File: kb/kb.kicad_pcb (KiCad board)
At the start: 2 copper layers, 109 parts, among them J1 Conn_01x04_MountingPin, SW1 SW_Push, SW10 SW_Push, SW11 SW_Push, SW12 SW_Push, SW13 SW_Push, SW14 SW_Push, SW15 SW_Push, SW16 SW_Push, SW17 SW_Push, SW18 SW_Push, SW19 SW_Push, SW2 SW_Push, SW20 SW_Push, SW21 SW_Push, SW22 SW_Push, SW23 SW_Push, SW24 SW_Push, SW25 SW_Push, SW26 SW_Push, SW27 SW_Push, SW28 SW_Push, SW29 SW_Push, SW3 SW_Push, SW30 SW_Push, SW31 SW_Push, SW32 SW_Push, SW33 SW_Push, SW34 SW_Push, SW35 SW_Push, SW36 SW_Push, SW37 SW_Push, SW38 SW_Push, SW39 SW_Push, SW4 SW_Push, SW40 SW_Push, SW41 SW_Push, SW42 SW_Push, SW43 SW_Push, SW44 SW_Push, SW45 SW_Push, SW46 SW_Push, SW48 SW_Push, SW5 SW_Push, SW6 SW_Push, SW7 SW_Push, SW8 SW_Push, SW9 SW_Push, U1 USBLC6-2SC6, U2 STM32G474CETx, U4 XC6206PxxxMR

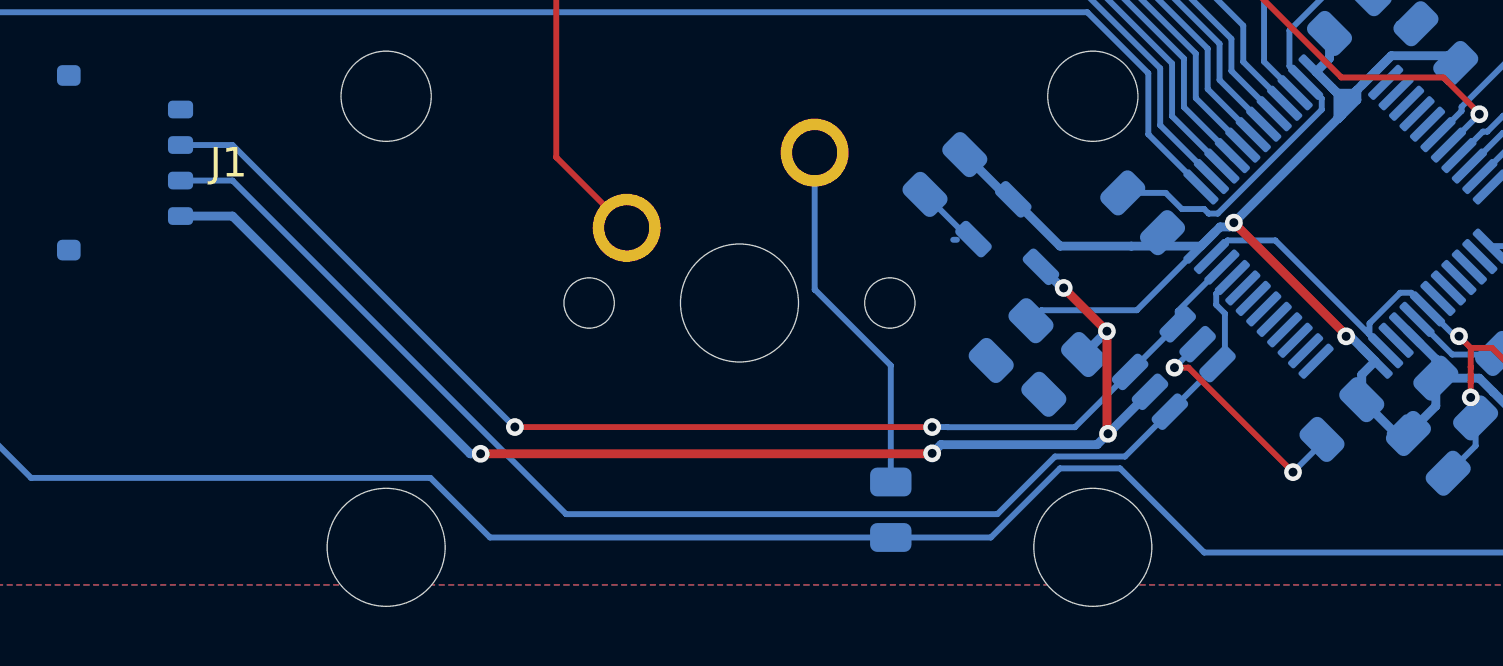
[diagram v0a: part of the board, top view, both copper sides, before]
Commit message: Removed ESD component
Due to built-in ESD functionality on daughterboard, onboard ESD protection is unnecessary
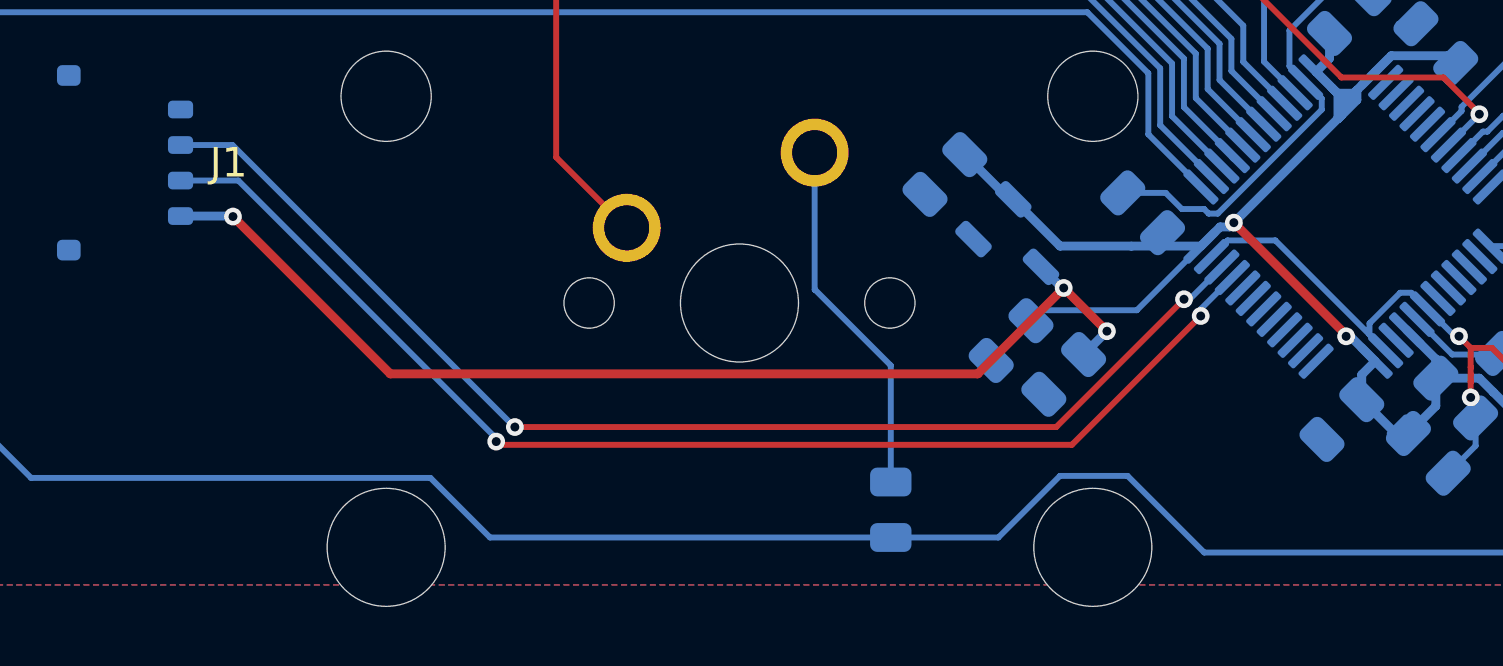
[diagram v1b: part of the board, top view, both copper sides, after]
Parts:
- removed U1: USBLC6-2SC6, Package_TO_SOT_SMD:SOT-23-6
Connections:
- C11 pad 2: (no net) -> GND
- C12 pad 2: (no net) -> GND
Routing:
- net GND: track 47.4 -> 37.1 mm, vias 5 -> 3
- net +5V: track 44.7 -> 37.5 mm, vias 5 -> 3
- net D-: track 45.2 -> 41.8 mm, vias 0 -> 2

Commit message: Added NSRT, Fixed Pins
Fixed boot pin and reset pin assignments, rerouted accordingly
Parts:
- moved C4 20.2 mm to (202.3, 102.4), turned to 180 degrees
- moved C10 18.3 mm to (195.6, 101.6), turned to 135 degrees
- moved C9 8.92 mm to (192.8, 101.6), turned to 135 degrees
- moved D42 8.87 mm to (181.0, 93.6)
- moved U4 8.85 mm to (190.1, 98.8), turned to -135 degrees
- moved J1 4.04 mm to (155.8, 93.5)
- moved C1 1.04 mm to (202.7, 98.9), turned to 45 degrees
- moved C5 1.02 mm to (187.5, 93.2), turned to -135 degrees
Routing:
- net GND: track 37.1 -> 53.2 mm
- net ROW3: track 255.9 -> 264.8 mm, vias 0 -> 2
- net +3V3: track 187.4 -> 179.5 mm, vias 4 -> 5
- net Net-(D42-A): track 12.2 -> 5.64 mm
- net D-: track 41.8 -> 36.2 mm, vias 2 -> 0
- net D+: track 41.4 -> 36.1 mm, vias 2 -> 0
- net ROW2: track 231.5 -> 235.1 mm
- net ROW0: track 280.6 -> 282.3 mm
- net Net-(U2-VREF+): track 6.61 -> 7.71 mm
- net COL0: track 219.9 -> 220.8 mm
- net +5V: track 37.5 -> 36.8 mm, vias 3 -> 0
- net ROW1: track 251.4 -> 250.8 mm

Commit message: Shrunk passive footprints
Switched footprint of passives from 0805  to 0402 and rewired accordingly
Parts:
- added C6: 100nF, Capacitor_SMD:C_0402_1005Metric, B.Cu at (198.1, 88.1)
- added SW47: RESET, Button_Switch_SMD:SW_SPST_SKQG_WithStem, B.Cu at (271.4, 33.9)
- C1, C10, C11, C12, C13, C2, C3, C4, C5, C8, C9: footprint Capacitor_SMD:C_0805_2012Metric -> Capacitor_SMD:C_0402_1005Metric
- R5: footprint Resistor_SMD:R_0805_2012Metric -> Resistor_SMD:R_0402_1005Metric
- SW48: value SW_Push -> BOOT
- moved R5 60.6 mm to (241.9, 30.5), turned to -90 degrees
- moved SW48 25.0 mm to (247.4, 34.3)
- moved C4 8.76 mm to (194.3, 98.8), turned to 0 degrees
- moved C1 4.11 mm to (199.6, 96.2), turned to -45 degrees
- moved C10 3.81 mm to (192.3, 99.7), turned to 45 degrees
- moved C9 2.74 mm to (190.1, 101.0)
- moved C3 2.69 mm to (194.7, 86.1)
- moved C12 2.18 mm to (197.6, 98.2)
- moved C13 2.17 mm to (196.3, 98.9), turned to -45 degrees
- moved C8 1.40 mm to (198.9, 96.9)
- moved C2 1.26 mm to (193.5, 86.4), turned to 135 degrees
- moved C11 0.95 mm to (198.2, 97.5)
- moved C5 0.95 mm to (188.4, 93.1)
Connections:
- U2 pad 13: ROW3 -> ROW2
- U2 pad 31: unconnected-(U2-PA9-Pad31) -> ROW3
- U2 pad 44: ROW0 -> COL7
- U2 pad 45: ROW1 -> BOOT
- U2 pad 46: ROW2 -> ROW1
- U2 pad 7: BOOT -> RESET
- U2 pad 8: COL7 -> ROW0
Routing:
- net RESET: track 0.00 -> 133.5 mm
- net GND: track 53.2 -> 30.4 mm, vias 3 -> 1
- net +3V3: track 179.5 -> 162.6 mm, vias 5 -> 4
- net BOOT: track 131.8 -> 123.3 mm, vias 0 -> 2
- net ROW0: track 282.3 -> 274.0 mm
- net ROW3: track 264.8 -> 257.1 mm, vias 2 -> 3
- net COL7: track 67.8 -> 61.4 mm
- net ROW2: track 235.1 -> 239.4 mm, vias 0 -> 2
- net Net-(U2-VREF+): track 7.71 -> 3.53 mm
- net +5V: track 36.8 -> 34.6 mm

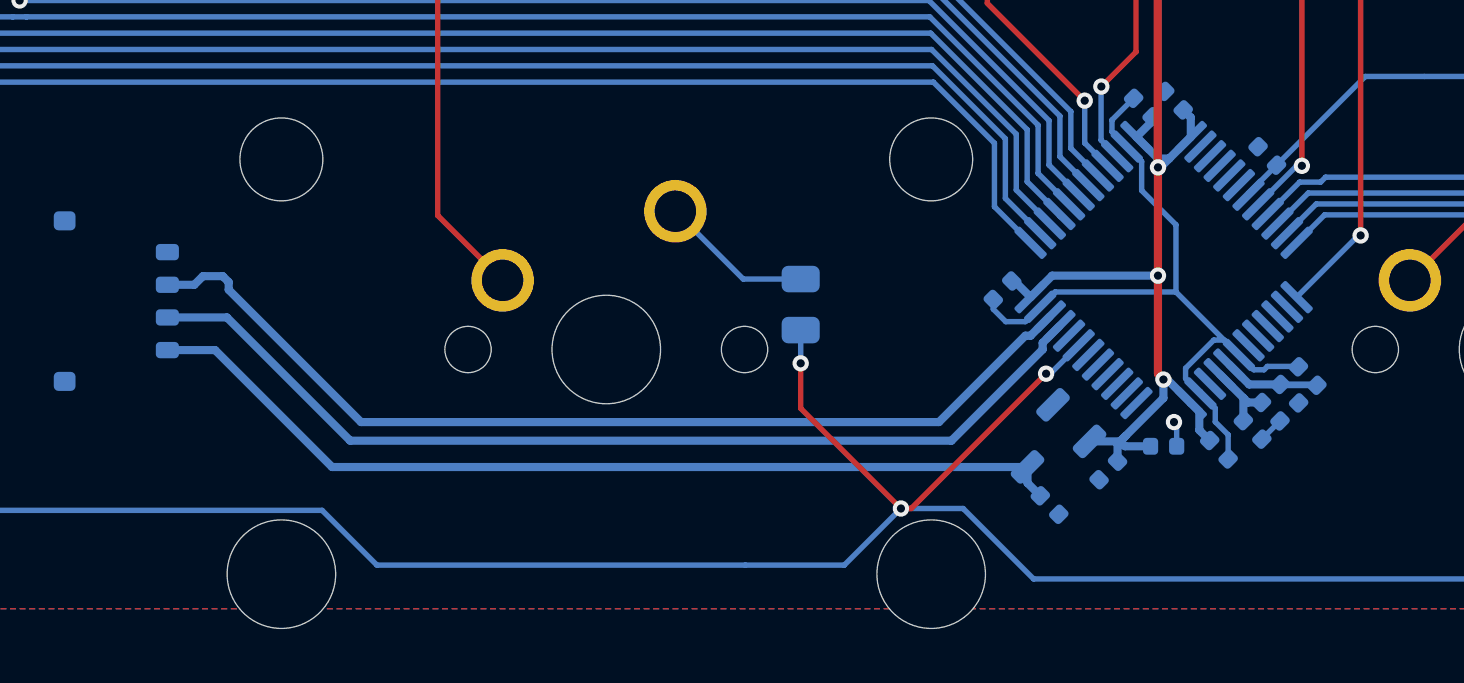
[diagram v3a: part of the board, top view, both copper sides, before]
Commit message: Moved LDO
 Moved LDO away from MCU for thermals, ensured all fills are grounded
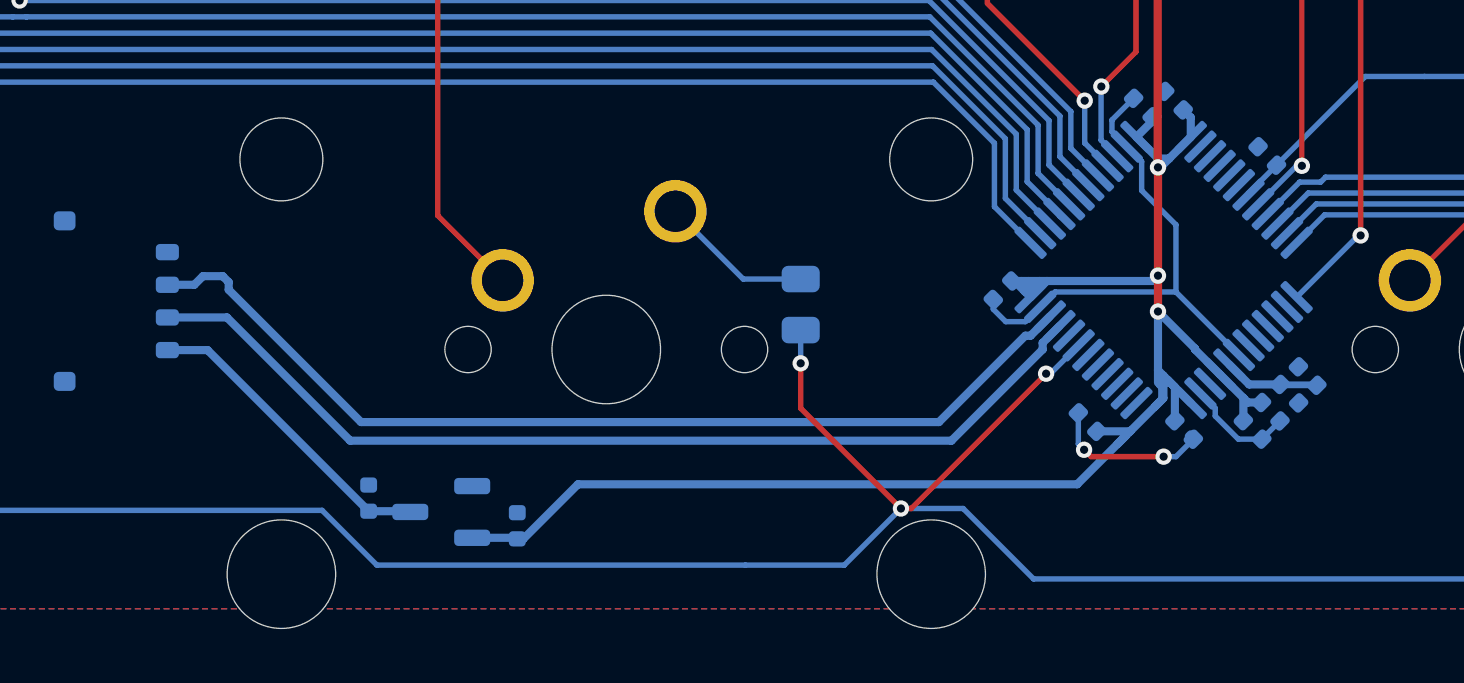
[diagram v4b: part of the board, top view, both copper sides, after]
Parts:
- moved C9 25.0 mm to (165.1, 100.7), turned to -90 degrees
- moved U4 22.5 mm to (167.8, 101.2), turned to 180 degrees
- moved C10 21.8 mm to (170.6, 101.7), turned to -90 degrees
- moved C4 2.93 mm to (191.5, 97.9), turned to 135 degrees
- moved C13 1.47 mm to (195.1, 98.2)
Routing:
- net +3V3: track 162.6 -> 194.1 mm
- net +5V: track 34.6 -> 11.4 mm
- net GND: track 30.4 -> 29.5 mm, vias 1 -> 2

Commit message: Layout Fix
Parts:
- moved C10 19.6 mm to (151.6, 96.8)
- moved C9 14.7 mm to (151.9, 94.2), turned to 0 degrees
- moved U4 14.6 mm to (154.1, 96.1), turned to 90 degrees
- moved J1 3.42 mm to (154.6, 90.3), turned to 0 degrees
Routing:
- net GND: track 29.5 -> 67.0 mm
- net +3V3: track 194.1 -> 211.3 mm
- net +5V: track 11.4 -> 4.05 mm
- net D+: track 36.5 -> 41.2 mm
- net D-: track 36.5 -> 41.1 mm

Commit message: Added edge cuts
Added edge cuts (dimensioned 82.325 x 256.525 mm, 1.5mm diameter fillet)
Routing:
- net GND: track 67.0 -> 29.5 mm
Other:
- board outline added: 256.5 x 82.3 mm
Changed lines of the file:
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@@
 		)
 	)
+	(gr_line
+		(start 276.775 107.825)
+		(end 23.25 107.825)
+		(stroke
+			(width 0.05)
+			(type default)
+		)
+		(layer "Edge.Cuts")
+	)
+	(gr_arc
+		(start 278.275 106.325)
+		(mid 277.83566 107.38566)
+		(end 276.775 107.825)
+		(stroke
+			(width 0.05)
+			(type default)
+		)
+		(layer "Edge.Cuts")
+	)
+	(gr_arc
+		(start 21.75 27)
+		(mid 22.18934 25.93934)
+		(end 23.25 25.5)
+		(stroke
+			(width 0.05)
+			(type default)
+		)
+		(layer "Edge.Cuts")
+	)
+	(gr_arc
+		(start 276.775 25.5)
+		(mid 277.83566 25.93934)
+		(end 278.275 27)
+		(stroke
+			(width 0.05)
+			(type default)
+		)
+		(layer "Edge.Cuts")
+	)
+	(gr_arc
+		(start 23.25 107.825)
+		(mid 22.18934 107.38566)
+		(end 21.75 106.325)
+		(stroke
+			(width 0.05)
+			(type default)
+		)
+		(layer "Edge.Cuts")
+	)
+	(gr_line
+		(start 278.275 27)
+		(end 278.275 106.325)
+		(stroke
+			(width 0.05)
+			(type default)
+		)
+		(layer "Edge.Cuts")
+	)
+	(gr_line
+		(start 21.75 106.325)
+		(end 21.75 27)
+		(stroke
+			(width 0.05)
+			(type default)
+		)
+		(layer "Edge.Cuts")
+	)
+	(gr_line
+		(start 23.25 25.5)
+		(end 276.775 25.5)
+		(stroke
+			(width 0.05)
+			(type default)
+		)
+		(layer "Edge.Cuts")
+	)
 	(segment
 		(start 40.64 33.02)
@@
 	)
 	(segment
-		(start 188.468 69.342)
-		(end 188.468 61.1175)
+		(start 189.3 70.174)
+		(end 193.294 74.168)
 		(width 0.2)
 		(layer "F.Cu")
@@
 	)
 	(segment
-		(start 192.398244 85.210244)
+		(start 193.294 74.168)
 		(end 193.294 84.314488)
 		(width 0.2)
@@
 	)
 	(segment
-		(start 193.294 74.168)
-		(end 188.468 69.342)
+		(start 193.294 84.314488)
+		(end 192.398244 85.210244)
 		(width 0.2)
 		(layer "F.Cu")
@@
 	)
 	(segment
-		(start 193.294 84.314488)
-		(end 193.294 74.168)
+		(start 189.3 61.1175)
+		(end 189.3 70.174)
 		(width 0.2)
 		(layer "F.Cu")
@@
 	)
 	(via
-		(at 188.468 61.1175)
+		(at 189.3 61.1175)
 		(size 0.6)
 		(drill 0.3)
@@
 	)
 	(segment
-		(start 147.955 61.1175)
-		(end 167.005 61.1175)
+		(start 186.055 61.1175)
+		(end 189.3 61.1175)
 		(width 0.2)
 		(layer "B.Cu")
@@
 	)
 	(segment
-		(start 71.755 61.1175)
-		(end 90.805 61.1175)
+		(start 147.955 61.1175)
+		(end 167.005 61.1175)
 		(width 0.2)
 		(layer "B.Cu")
@@
 	)
 	(segment
-		(start 188.468 61.1175)
-		(end 205.105 61.1175)
+		(start 71.755 61.1175)
+		(end 90.805 61.1175)
 		(width 0.2)
 		(layer "B.Cu")
@@
 	)
 	(segment
-		(start 186.055 61.1175)
-		(end 188.468 61.1175)
-		(width 0.2)
-		(layer "B.Cu")
-		(net 14)
-	)
-	(segment
 		(start 205.105 61.1175)
 		(end 224.155 61.1175)
@@
 	)
 	(segment
+		(start 189.3 61.1175)
+		(end 205.105 61.1175)
+		(width 0.2)
+		(layer "B.Cu")
+		(net 14)
+	)
+	(segment
 		(start 192.398244 85.210244)
 		(end 192.012251 85.596237)
@@
 	)
 	(segment
-		(start 189.702178 99.052)
-		(end 191.176589 97.577589)
-		(width 0.2)
-		(layer "B.Cu")
-		(net 62)
-	)
-	(segment
 		(start 197.919375 98.543836)
 		(end 197.919375 98.542447)
@@
 	)
 	(segment
-		(start 156.776499 99.052)
-		(end 189.702178 99.052)
-		(width 0.2)
-		(layer "B.Cu")
-		(net 62)
-	)
-	(segment
 		(start 196.207749 97.696296)
 		(end 196.207749 97.408729)
@@
 	)
 	(segment
-		(start 155.000999 97.2765)
-		(end 156.776499 99.052)
-		(width 0.2)
-		(layer "B.Cu")
-		(net 62)
-	)
-	(segment
 		(start 189.230271 94.226749)
 		(end 189.775678 93.681342)
@@
 	)
 	(segment
-		(start 187.579 34.29)
-		(end 191.897 29.972)
+		(start 187.579 33.571)
+		(end 187.579 71.374)
+		(width 0.2)
+		(layer "F.Cu")
+		(net 69)
+	)
+	(segment
+		(start 188.722 72.517)
+		(end 188.722 74.295)
 		(width 0.2)
 		(layer "F.Cu")
@@
 	(segment
 		(start 187.579 71.374)
-		(end 187.579 34.29)
+		(end 188.722 72.517)
 		(width 0.2)
 		(layer "F.Cu")
@@
 	)
 	(segment
-		(start 188.722 72.517)
-		(end 187.579 71.374)
+		(start 187.833 75.184)
+		(end 187.833 79.783)
 		(width 0.2)
 		(layer "F.Cu")
@@
 	)
 	(segment
-		(start 190.909526 84.396996)
-		(end 187.833 81.32047)
+		(start 191.2 29.95)
+		(end 187.579 33.571)
 		(width 0.2)
 		(layer "F.Cu")
@@
 	)
 	(segment
-		(start 187.833 81.32047)
+		(start 188.722 74.295)
 		(end 187.833 75.184)
 		(width 0.2)
@@
 	)
 	(segment
-		(start 187.833 75.184)
-		(end 188.722 74.295)
+		(start 190.909526 82.859526)
+		(end 190.909526 84.396996)
 		(width 0.2)
 		(layer "F.Cu")
@@
 	)
 	(segment
-		(start 188.722 74.295)
-		(end 188.722 72.517)
+		(start 187.833 79.783)
+		(end 190.909526 82.859526)
 		(width 0.2)
 		(layer "F.Cu")
@@
 	)
 	(via
-		(at 191.897 29.972)
+		(at 191.2 29.95)
 		(size 0.6)
 		(drill 0.3)
@@
 	)
 	(segment
-		(start 191.897 29.972)
-		(end 239.903 29.972)
-		(width 0.2)
-		(layer "B.Cu")
-		(net 69)
-	)
-	(segment
 		(start 243.28 31.19)
 		(end 245.546 31.19)
@@
 	)
 	(segment
+		(start 191.2 29.95)
+		(end 191.222 29.972)
+		(width 0.2)
+		(layer "B.Cu")
+		(net 69)
+	)
+	(segment
 		(start 239.905 29.97)
-		(end 239.903 29.972)
+		(end 241.935 29.97)
 		(width 0.2)
 		(layer "B.Cu")
@@
 	(segment
 		(start 241.935 29.97)
+		(end 242.06 29.97)
+		(width 0.2)
+		(layer "B.Cu")
+		(net 69)
+	)
+	(segment
+		(start 239.903 29.972)
 		(end 239.905 29.97)
 		(width 0.2)
@@
 	)
 	(segment
-		(start 241.935 29.97)
-		(end 242.06 29.97)
+		(start 191.222 29.972)
+		(end 239.903 29.972)
 		(width 0.2)
 		(layer "B.Cu")
@@
 		(polygon
 			(pts
-				(xy 24.003 28.575) (xy 23.876 104.775) (xy 276.225 104.775) (xy 276.225 28.575)
+				(xy 277.792568 25.964432) (xy 149.350453 26.175309) (xy 22.21557 25.96557) (xy 22.2267 107.379843)
+				(xy 277.817294 107.383294)
 			)
 		)
